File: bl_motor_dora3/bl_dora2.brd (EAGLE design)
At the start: 85 x 50.8 mm, 78 parts

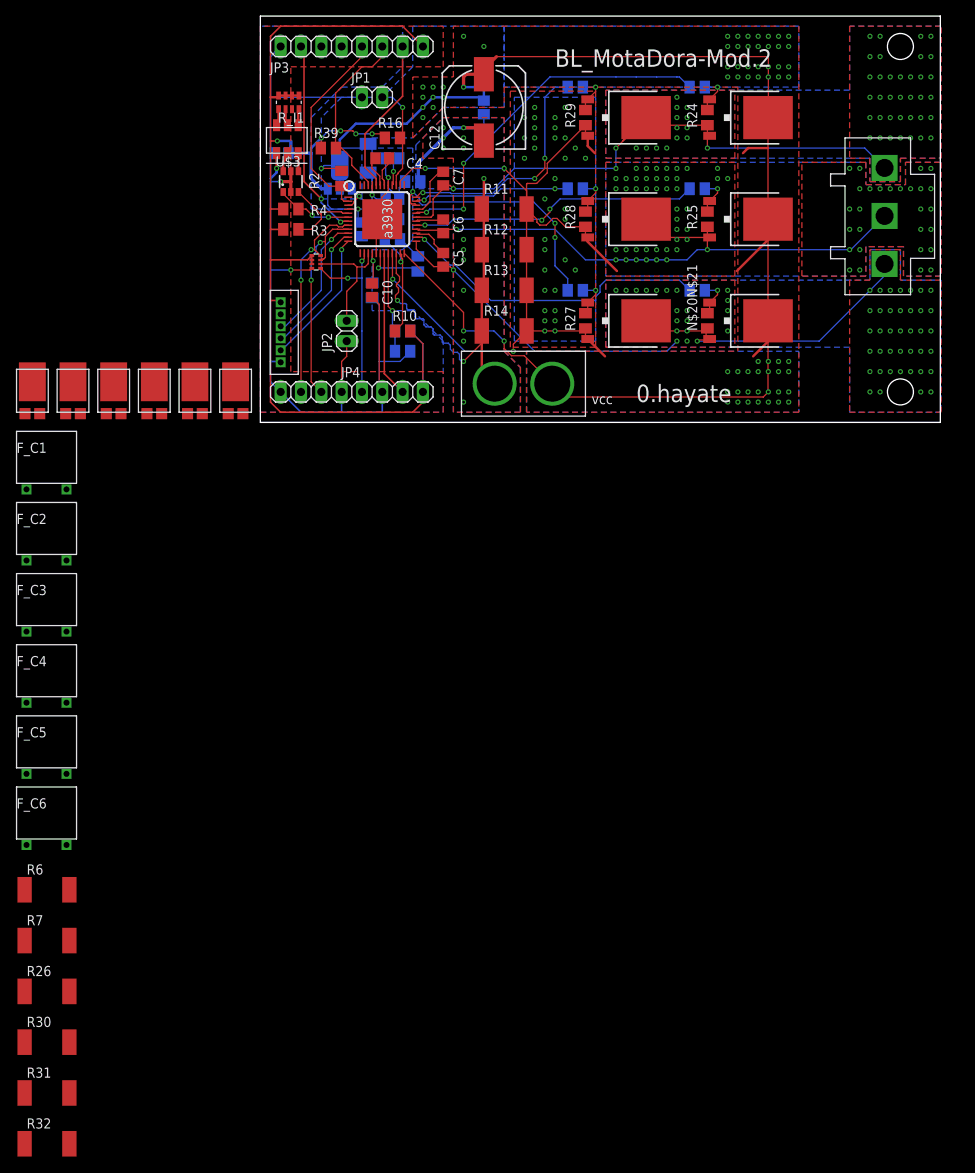
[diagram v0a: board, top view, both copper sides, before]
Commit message: 一応完成したもの
fetにスナバ回路を加えることによりモーターサージを吸収できるようにした。ゲート・ソース間にコンデンサを入れられるようにして、セルフターンオンしないように細かく調整できるようにした。デッドタイムの設計を変え忘れた。確か47kΩでデッドタイムが700nSecほどになる。空冷するためのファン用のコネクタを追加した。還流ダイオードを入れるスペースが作れなかった。この設計で実験し思う性能が出せない場合は基板サイズを犠牲にするか4層化し、知っている限りの保護回路をマシマシにする。
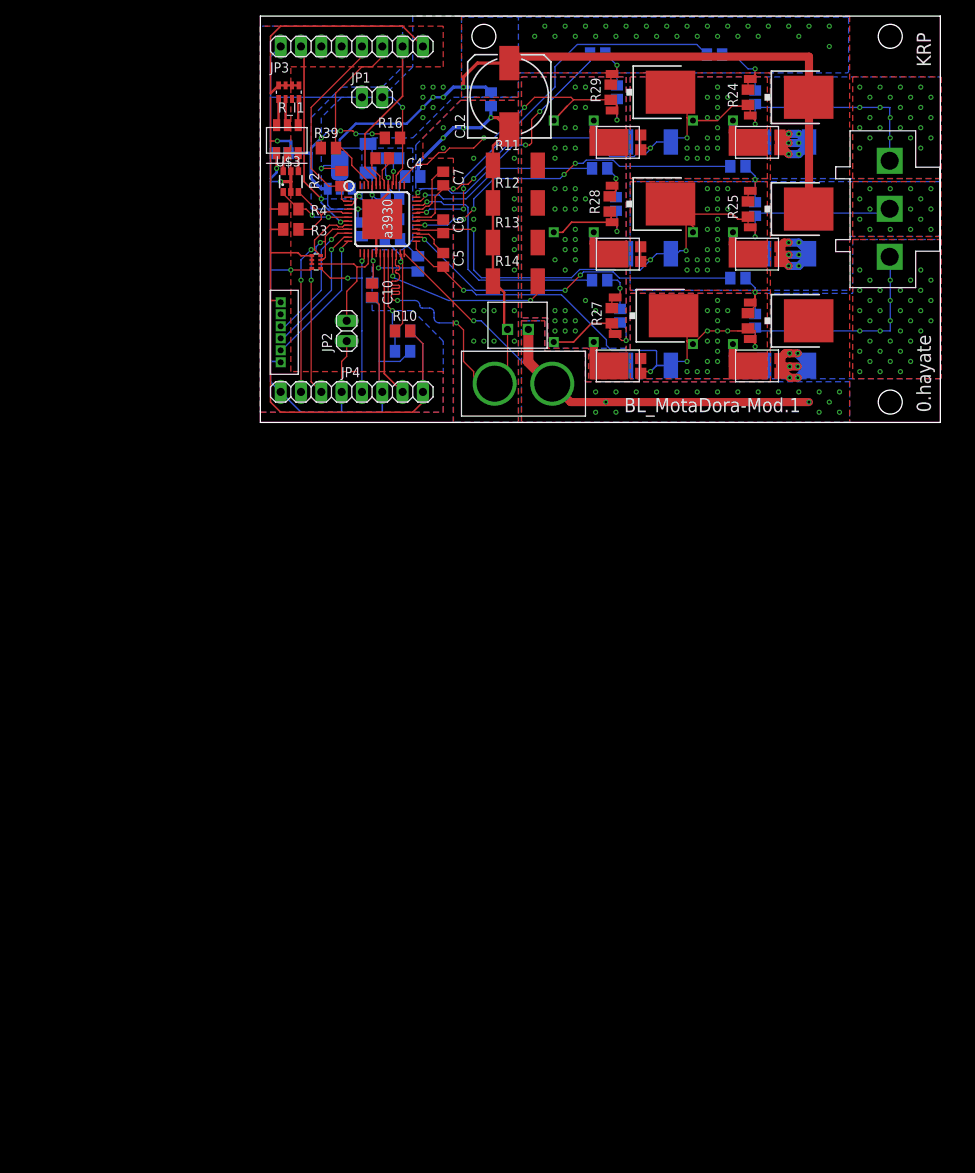
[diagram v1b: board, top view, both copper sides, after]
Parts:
- added C13, C14, C15, C16, C17, C18: (no value), rcl:C2012
- added U$19: XH_2P, user:XH_2P
- moved R7 136.1 mm to (65.8, 35.1), flipped to the bottom, turned to 180 degrees
- moved R30 135.1 mm to (65.8, 21.1), flipped to the bottom, turned to 180 degrees
- moved R31 129.7 mm to (65.8, 7.11), flipped to the bottom, turned to 180 degrees
- moved R32 122.9 mm to (48.5, 7.11), flipped to the bottom, turned to 180 degrees
- moved F_C5 122.1 mm to (60.3, 38.5), flipped to the bottom
- moved R6 120.0 mm to (48.5, 35.1), flipped to the bottom, turned to 180 degrees
- moved R26 119.0 mm to (48.5, 21.1), flipped to the bottom, turned to 180 degrees
- moved F_C6 116.6 mm to (42.9, 38.5), flipped to the bottom
- moved F_C4 108.2 mm to (60.3, 24.5), flipped to the bottom
- moved F_C3 97.7 mm to (60.3, 10.5), flipped to the bottom
- moved U$17 90.3 mm to (64.8, 5.08), turned to 90 degrees
- moved U$16 86.9 mm to (64.8, 19.1), turned to 90 degrees
- moved F_C2 84.1 mm to (42.9, 24.5), flipped to the bottom
- moved U$18 77.9 mm to (47.4, 5.08), turned to 90 degrees
- moved U$13 76.7 mm to (64.8, 33.0), turned to 90 degrees
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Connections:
- net GND: now also U$19.P$1
- net N$19: now also C13.2
- net N$25: now also C13.1
- net N$26: now also C18.1
- net N$27: now also C17.1
- net N$28: now also C16.1
- net N$29: now also C15.1
- net N$30: now also C14.1
- net N$4: now also C17.2
- net N$50: now also C18.2
- net N$8: now also C14.2, C15.2, C16.2
- net VCC: now also U$19.P$2
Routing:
- net N$4: track 79.1 -> 96.0 mm, vias 61 -> 58
- net VCC: track 196.6 -> 212.5 mm, vias 68 -> 79
- net N$19: track 74.0 -> 89.8 mm, vias 53 -> 48
- net N$8: track 107.8 -> 93.3 mm, vias 37 -> 43
- net N$50: track 75.5 -> 89.5 mm, vias 3 -> 39
- net N$40: track 0.00 -> 11.2 mm
- net GND: track 73.1 -> 84.0 mm, vias 15 -> 23
- net N$39: track 0.00 -> 10.4 mm
- net N$5: track 0.00 -> 9.87 mm
- net N$42: track 0.00 -> 9.87 mm
- net N$38: track 0.00 -> 9.85 mm
- net N$9: track 0.00 -> 9.85 mm
- net N$36: track 36.4 -> 43.7 mm, vias 3 -> 5
- net N$25: track 4.98 -> 10.5 mm
- net N$32: track 19.6 -> 24.2 mm, vias 2 -> 1
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- added copper zone on layer 1, net N$50
- added copper zone on layer 16, net N$50
- removed copper zone on layer 1, net N$20
- removed copper zone on layer 16, net N$20
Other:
- board text added: "BL_MotaDora-Mod.1"
- board text added: "KRP"
- board text removed: "BL_MotaDora-Mod.2"
- board text removed: "vcc"

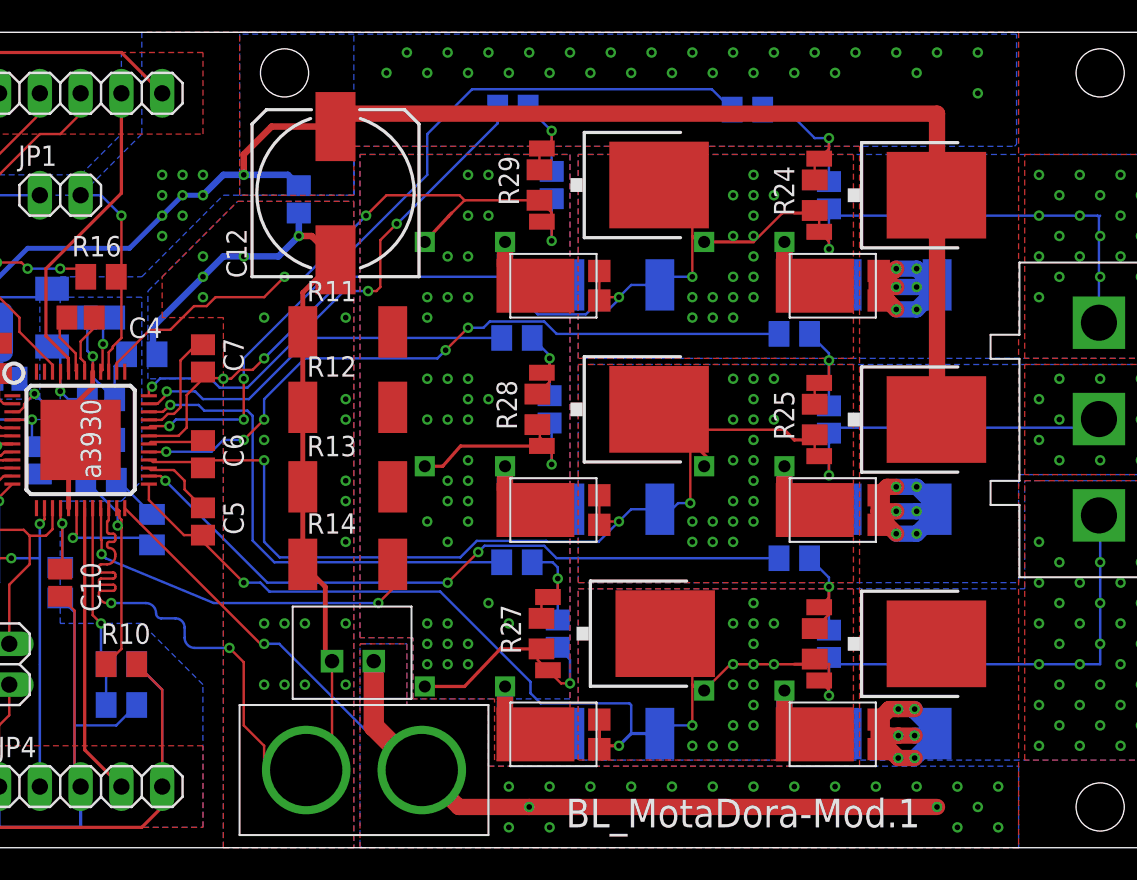
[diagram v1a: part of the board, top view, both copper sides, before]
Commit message: フィードバックを受けて修正したもの
スナバを大幅に修正して非放電型スナバにした。これにより抵抗器の損失を少なくできるため小型の抵抗器が使えるようになった。スナバに使っていたダイオードを還流ダイオードに使用して、スナバのダイオードは小さめのものに変えた。電流センサ用の配線をくねくねしないで揃うように頑張った。非放電型スナバの周りの配線が複雑になって怪しい気がするのでチェックお願いします。
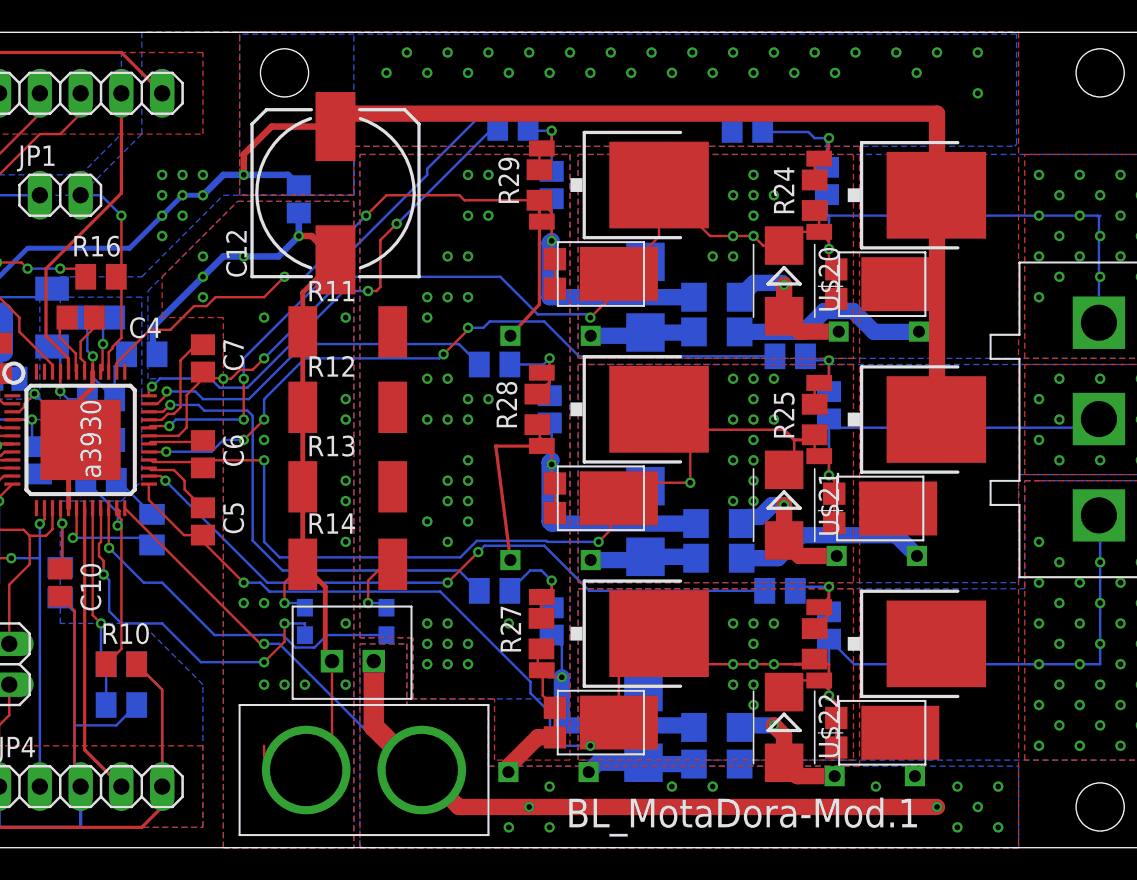
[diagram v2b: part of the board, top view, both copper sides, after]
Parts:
- added R33, R34: 0, user:1608REG
- added U$20, U$21, U$22, U$26, U$27, U$28: ES3BB13F, user:ES3BB13F
- C13, C14, C15, C16, C17, C18: value (none) -> 5n
- C5, C6, C7: value 0.1u -> 0.22u
- R15: value 100k -> 33k
- R18, R19, R20, R21, R22, R23: value 47 -> 10
- R26, R30, R31, R32, R6, R7: device rcl:R2512 -> rcl:R1206
- R29: value 10jk -> 10k
- R3, R4: value 4.7k -> 10k
- moved R32 27.9 mm to (54.9, 34.3)
- moved R7 20.2 mm to (55.0, 18.0)
- moved R30 17.4 mm to (54.9, 7.49)
- moved R26 17.1 mm to (54.9, 5.21)
- moved R31 17.0 mm to (55.0, 20.2)
- moved F_C5 10.1 mm to (68.7, 32.9)
- moved F_C4 9.97 mm to (68.6, 18.9)
- moved F_C3 9.72 mm to (68.5, 5.21)
- moved F_C2 7.91 mm to (48.3, 18.7)
- moved F_C6 7.91 mm to (48.3, 32.6)
- moved F_C1 7.45 mm to (48.1, 5.46)
- moved R6 6.99 mm to (54.9, 32.1)
- moved U$18 5.28 mm to (45.0, 9.78), turned to 270 degrees
- moved U$14 5.28 mm to (45.0, 37.7), turned to 270 degrees
- moved U$15 5.28 mm to (45.0, 23.7), turned to 270 degrees
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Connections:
- removed net N$39: F_C1.P$1, R32.1, U$18.K
- removed net N$4: C17.2, C5.2, F_C3.P$2, N$20N$21.1, R32.2, U$1.PIN25, U$11.PIN3_S, U$12.PIN2_D, U$18.A1, U$18.A2, U$25.P$3
- removed net N$8: C14.2, C15.2, C16.2, F_C1.P$2, F_C2.P$2, F_C6.P$2, R11.2, R12.2, R13.2, R14.2, R27.1, R28.1, R29.1, U$1.PIN21, U$1.PIN38, U$10.PIN3_S, U$12.PIN3_S, U$8.PIN3_S
- removed net N$9: F_C6.P$1, R6.1, U$14.K
- new net N$10: R33.2, U$1.PIN22
- new net N$20: R34.2, U$1.PIN21
- new net N$41: F_C3.P$2, R30.2, U$22.A
- new net N$44: C17.2, C5.2, N$20N$21.1, U$1.PIN25, U$11.PIN3_S, U$12.PIN2_D, U$17.A1, U$17.A2, U$18.K, U$22.C, U$25.P$3, U$28.A
- new net N$45: F_C1.P$1, R26.1, U$28.C
- new net N$47: F_C2.P$1, R7.1, U$27.C
- net GND: now also R34.1; no longer U$1.PIN22
- net N$19: now also U$13.A1, U$13.A2, U$14.K, U$20.C, U$26.A; no longer F_C5.P$2, R6.2, U$14.A1, U$14.A2
- net N$38: now also F_C4.P$2, R31.2, U$21.A; no longer F_C2.P$1, R26.1, U$15.K
- net N$40: now also C14.2, C15.2, C16.2, F_C1.P$2, F_C2.P$2, F_C6.P$2, R11.2, R12.2, R13.2, R14.2, R27.1, R28.1, R29.1, R30.1, R32.1, R33.1, U$1.PIN38, U$10.PIN3_S, U$12.PIN3_S, U$14.A1, U$14.A2, U$15.A1, U$15.A2, U$18.A1, U$18.A2, U$8.PIN3_S; no longer F_C3.P$1, U$17.K
- net N$42: now also F_C6.P$1, R6.1, U$26.C; no longer F_C4.P$1, R30.1, U$16.K
- net N$5: now also F_C5.P$2, R32.2, U$20.A; no longer F_C5.P$1, R7.1, U$13.K
- net N$50: now also U$15.K, U$16.A1, U$16.A2, U$21.C, U$27.A; no longer F_C4.P$2, R26.2, U$15.A1, U$15.A2
- net VCC: now also F_C3.P$1, F_C4.P$1, F_C5.P$1, R26.2, R6.2, U$13.K, U$16.K, U$17.K; no longer R30.2, R31.2, U$13.A1, U$13.A2, U$16.A1, U$16.A2, U$17.A1, U$17.A2
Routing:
- net N$40: track 11.2 -> 124.6 mm, vias 0 -> 40
- net N$44: track 0.00 -> 96.3 mm, vias 0 -> 51
- net N$4: track 96.0 -> 0.00 mm, vias 58 -> 0
- net N$8: track 93.3 -> 0.00 mm, vias 43 -> 0
- net GND: track 84.0 -> 59.9 mm, vias 23 -> 21
- net N$10: track 0.00 -> 22.7 mm, vias 0 -> 1
- net N$20: track 0.00 -> 22.6 mm, vias 0 -> 3
- net VCC: track 212.5 -> 192.1 mm, vias 79 -> 54
- net N$39: track 10.4 -> 0.00 mm
- net N$9: track 9.85 -> 0.00 mm
- net N$41: track 0.00 -> 8.27 mm, vias 0 -> 1
- net N$45: track 0.00 -> 6.84 mm
- net N$47: track 0.00 -> 6.68 mm
- net N$42: track 9.87 -> 6.53 mm
- net N$35: track 49.3 -> 47.5 mm
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- added copper zone on layer 1, net N$40
- added copper zone on layer 16, net N$40
- added copper zone on layer 1, net N$44
- added copper zone on layer 16, net N$44
- removed copper zone on layer 1, net N$4
- removed copper zone on layer 16, net N$4
- removed copper zone on layer 1, net N$8
- removed copper zone on layer 16, net N$8

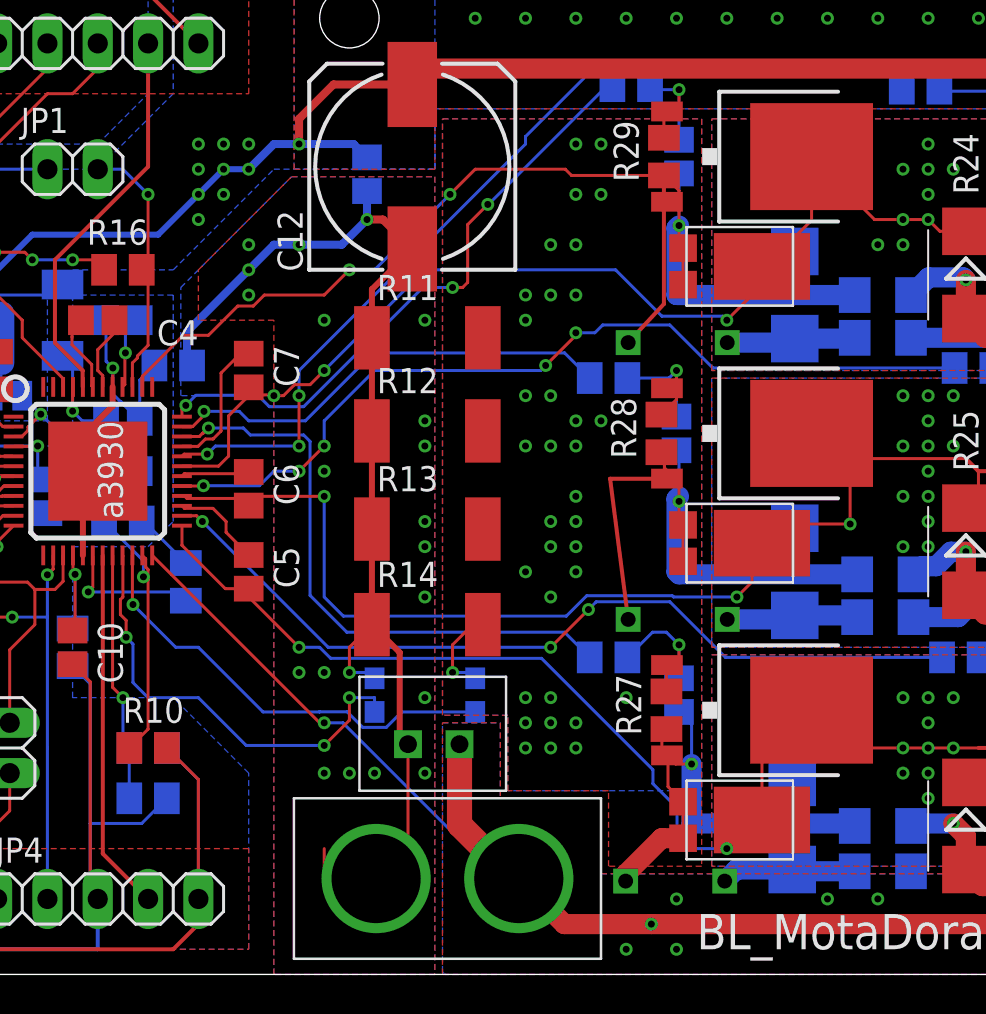
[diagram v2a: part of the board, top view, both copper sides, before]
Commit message: 配線修正
シャントの配線をしっかり切り分ける。
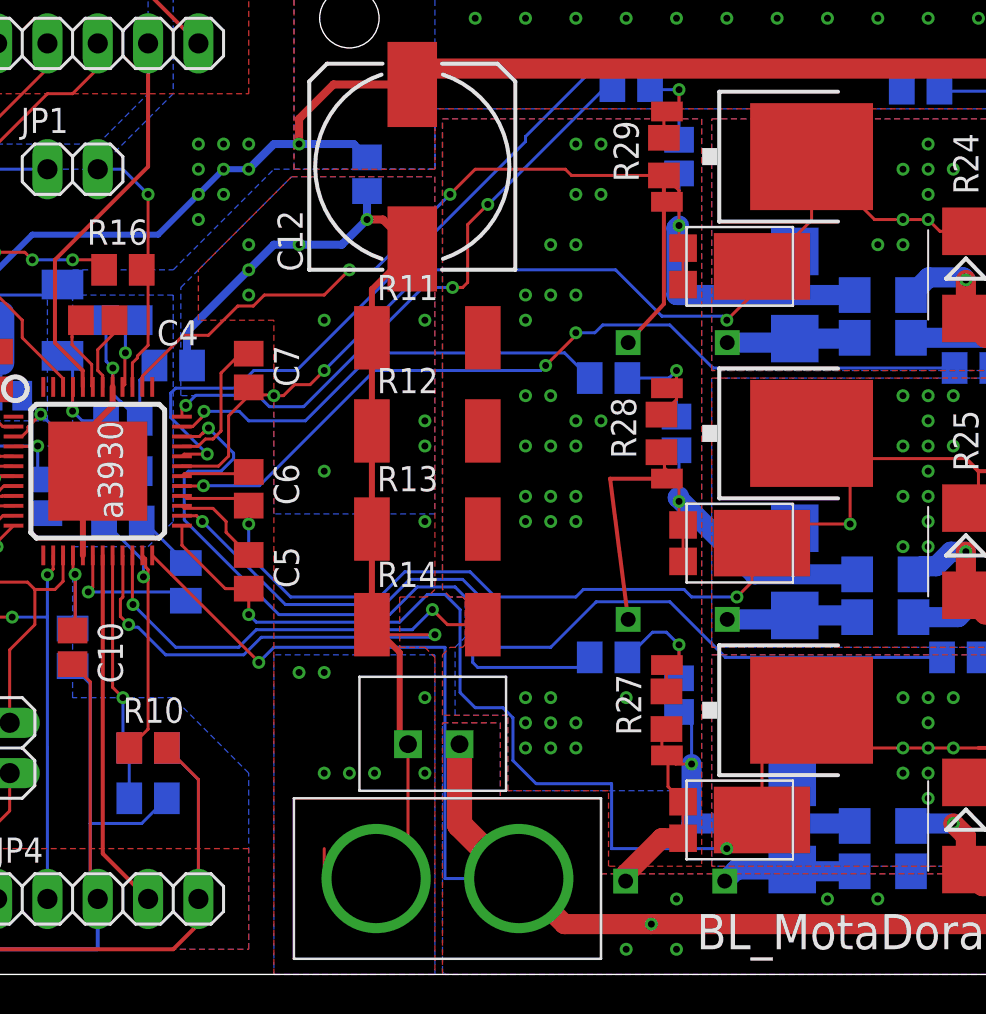
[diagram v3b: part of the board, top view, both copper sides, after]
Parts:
- removed R33, R34: 0, user:1608REG
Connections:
- removed net N$10: R33.2, U$1.PIN22
- removed net N$20: R34.2, U$1.PIN21
- net GND: now also U$1.PIN21; no longer R34.1
- net N$40: now also U$1.PIN22; no longer R33.1
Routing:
- net N$10: track 22.7 -> 0.00 mm, vias 1 -> 0
- net N$20: track 22.6 -> 0.00 mm, vias 3 -> 0
- net GND: track 59.9 -> 79.2 mm, vias 21 -> 20
- net N$40: track 124.6 -> 140.1 mm, vias 40 -> 39
- net VCC: track 192.1 -> 199.6 mm
- net N$44: track 96.3 -> 102.6 mm
- net N$33: track 30.1 -> 35.3 mm
- net N$37: track 43.2 -> 45.5 mm, vias 3 -> 1
- net N$35: track 47.5 -> 49.6 mm, vias 3 -> 1
- net N$50: track 89.0 -> 87.6 mm
- net N$36: track 44.1 -> 43.3 mm, vias 5 -> 3
